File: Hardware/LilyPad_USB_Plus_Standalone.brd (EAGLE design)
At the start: 50.7 x 50.7 mm, 114 parts, among them J1 SEWTAP_LONG-2SIDE, J10 SEWTAP_LONG-2SIDE, J11 SEWTAP_LONG-2SIDE, J12 SEWTAP_LONG-2SIDE, J13 SEWTAP_LONG-2SIDE, J14 SEWTAP_LONG-2SIDE, J15 AMP FCI 10103594-0001LF, J2 SEWTAP_LONG-2SIDE, J3 SEWTAP_LONG-2SIDE, J4 SEWTAP_LONG-2SIDE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

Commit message: Cleaned up some things
Ready for proto review
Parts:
- removed U$51, U$52, U$55, U$56, U$57, U$58, U$59, U$60, U$61, U$62, U$63, U$64, U$65, U$66, U$67: (no value), newLilypadParts:ROUTE_TICKS
- moved LOGO1 6.94 mm to (31.5, 11.4)
- moved LOGO6 6.35 mm to (24.9, 19.3)
- moved C3 1.27 mm to (35.0, 38.8)
- moved C5 1.27 mm to (24.6, 34.8)
- moved C6 1.27 mm to (40.8, 28.7)
- moved J12 1.27 mm to (46.3, 32.2)
- moved J14 1.27 mm to (34.3, 45.5)
- moved J9 1.27 mm to (38.3, 7.60)
- moved JP3 1.27 mm to (41.4, 34.5)
- moved S1 1.27 mm to (37.7, 20.3)
- moved TP7 1.27 mm to (36.2, 14.5)
- moved U$10 1.27 mm to (46.3, 32.2)
- moved U$11 1.27 mm to (46.3, 32.2)
- moved U$24 1.27 mm to (38.3, 7.60)
- moved U$25 1.27 mm to (38.3, 7.60)
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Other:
- board text added: "Inches"
- board text added: "Plated holes: 0.11"
- board text added: "Unplated holes: 0.013"
- board text added: "v01"
- board text removed: "v10"

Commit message: Small changes after Review
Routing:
- net GND: track 38.1 -> 42.7 mm, vias 21 -> 22
- net D3: track 41.7 -> 44.8 mm, vias 2 -> 3
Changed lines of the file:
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@@
 <layer number="47" name="Measures" color="7" fill="1" visible="no" active="yes"/>
 <layer number="48" name="Document" color="7" fill="1" visible="no" active="no"/>
-<layer number="49" name="Reference" color="13" fill="1" visible="no" active="yes"/>
+<layer number="49" name="Reference" color="13" fill="1" visible="yes" active="yes"/>
 <layer number="50" name="dxf" color="7" fill="1" visible="no" active="no"/>
 <layer number="52" name="bDocu" color="7" fill="1" visible="no" active="no"/>
@@
 <wire x1="29.501134375" y1="33.006678125" x2="29.4878125" y2="33.02" width="0.2032" layer="1"/>
 <contactref element="TP5" pad="P$1"/>
+<via x="0.762" y="22.606" extent="1-16" drill="0.3302"/>
+<wire x1="3.550275" y1="23.104434375" x2="1.965328125" y2="23.104434375" width="0.254" layer="16"/>
+<wire x1="0.762" y1="22.606" x2="3.051840625" y2="22.606" width="0.254" layer="16"/>
+<wire x1="3.051840625" y1="22.606" x2="3.550275" y2="23.104434375" width="0.254" layer="16"/>
 </signal>
 <signal name="N$3">
@@
 <wire x1="27.559" y1="39.9415" x2="29.130625" y2="41.513125" width="0.2032" layer="16"/>
 <wire x1="31.958865625" y1="37.6265" x2="31.958865625" y2="38.308865625" width="0.2032" layer="1"/>
+<via x="1.905" y="33.274" extent="1-16" drill="0.3302"/>
+<wire x1="4.496146875" y1="32.2007125" x2="4.50655" y2="32.190309375" width="0.254" layer="16"/>
+<wire x1="1.905" y1="33.274" x2="3.422859375" y2="33.274" width="0.254" layer="16"/>
+<wire x1="3.422859375" y1="33.274" x2="4.50655" y2="32.190309375" width="0.254" layer="16"/>
 </signal>
 <signal name="D9">

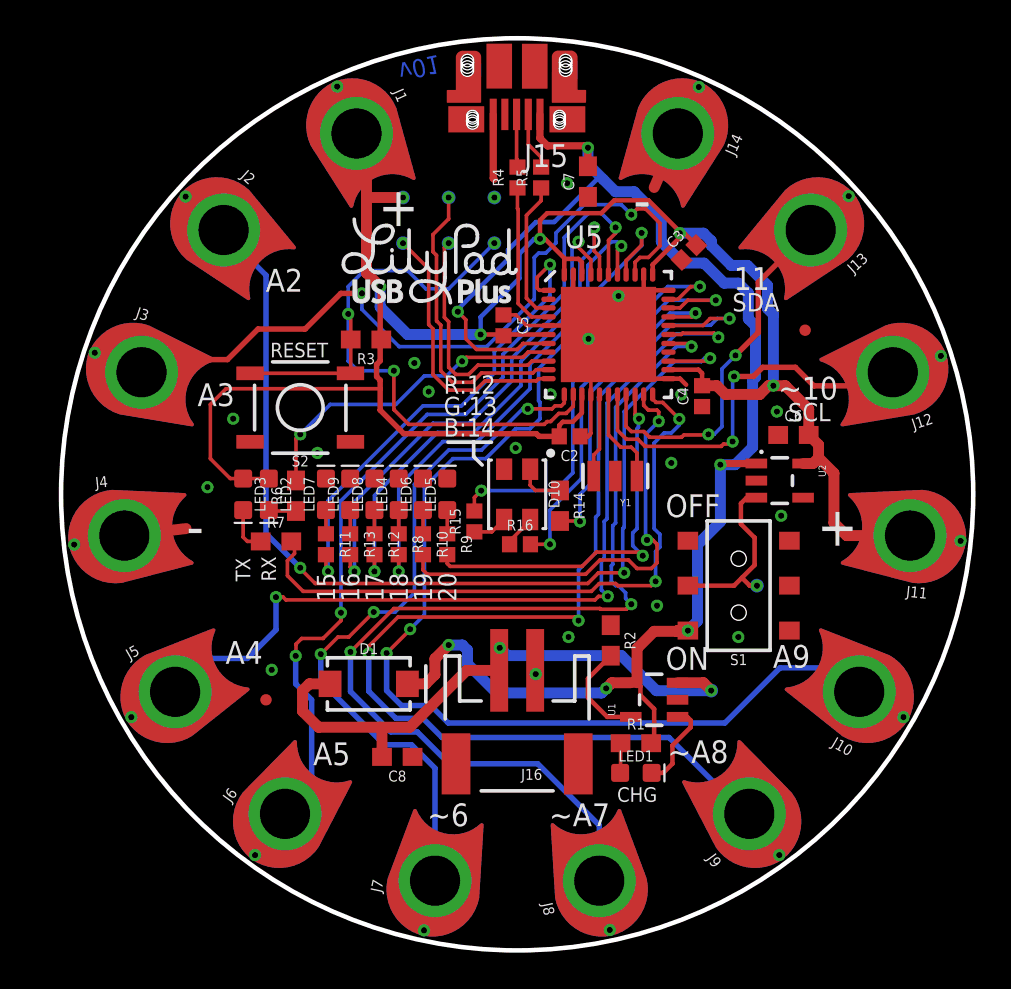
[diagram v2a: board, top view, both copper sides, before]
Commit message: Issues found from my double check
Fiducials on underside placed, Sparkfun name on board changed to flame according to Lilypad design rules.
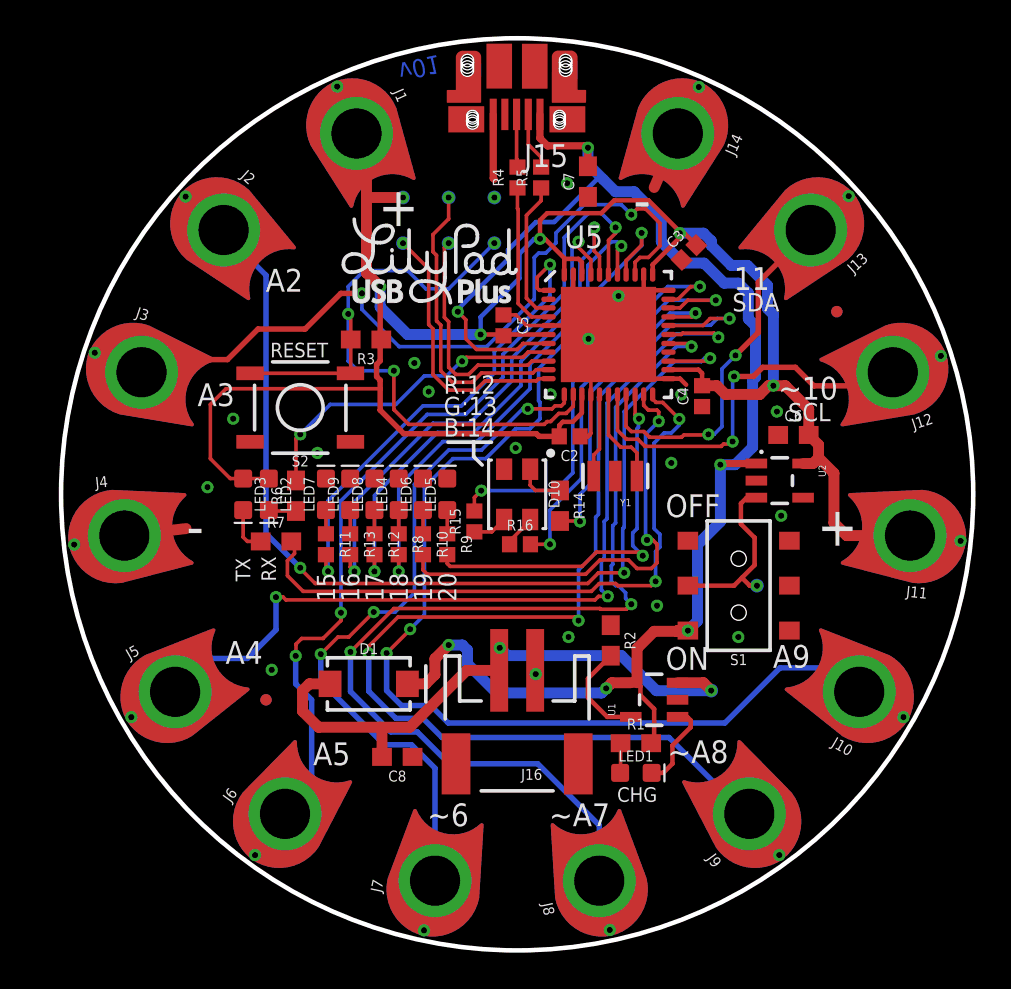
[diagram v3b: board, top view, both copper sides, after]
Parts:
- added JP1, JP4: FIDUCIALUFIDUCIAL, SparkFun:MICRO-FIDUCIAL
- LOGO1: value SFE_LOGO_NAME_FLAME.1_INCH -> SFE_LOGO_FLAME.2_INCH; device SparkFun-Aesthetics:SFE_LOGO_NAME_FLAME_.1 -> SparkFun-Aesthetics:SFE_LOGO_FLAME_.2
- moved LOGO6 12.3 mm to (25.5, 31.6)
- moved LOGO1 9.02 mm to (26.7, 19.1)
- moved JP3 2.04 mm to (43.2, 35.6)
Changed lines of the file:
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@@
 <dimension x1="50.79999375" y1="25.4" x2="0.00000625" y2="25.4" x3="25.4" y3="60.96" textsize="1.778" textratio="15" layer="47" unit="inch"/>
 <text x="29.845" y="61.722" size="1.778" layer="47" font="vector" ratio="15">Inches</text>
-<text x="5.08" y="-14.76375" size="1.778" layer="51" font="vector" align="top-left">LilyPad concept and shapes by:  L. Buechley and N. Seidle</text>
+<text x="-5.08" y="-14.76375" size="1.778" layer="52" font="vector" rot="MR0" align="top-left">LilyPad concept and shapes by:  L. Buechley and N. Seidle</text>
+<text x="-5.08" y="-30.48" size="1.778" layer="52" rot="MR0" align="top-left">PCB thickness: 31 mil / 0.8mm </text>
+<text x="-5.08" y="-34.29" size="1.778" layer="52" rot="MR0" align="top-left">Solder mask color: Purple (Lilypad)</text>
+<text x="-5.08" y="-38.1" size="1.778" layer="52" rot="MR0" align="top-left">Finishing: Lead-free HASL</text>
+<text x="-5.08" y="-41.91" size="1.778" layer="52" rot="MR0" align="top-left">Unplated holes:
+0.013
+</text>
+<text x="-31.75" y="-41.91" size="1.778" layer="52" rot="MR0" align="top-left">Plated holes:
+0.11
+</text>
+<text x="-52.07" y="-11.43" size="1.778" layer="52" font="vector" rot="MR0">Marshall Taylor</text>
+<text x="-32.131" y="-13.97" size="1.778" layer="52" font="vector" rot="MR0">Revised by: Elias Santistevan</text>
+<text x="3.81" y="-14.76375" size="1.778" layer="51" font="vector" align="top-left">LilyPad concept and shapes by:  L. Buechley and N. Seidle</text>
+<text x="50.8" y="-11.43" size="1.778" layer="51" font="vector">Marshall Taylor</text>
+<text x="32.131" y="-13.97" size="1.778" layer="51" font="vector">Revised by: Elias Santistevan</text>
 <text x="5.08" y="-30.48" size="1.778" layer="51" align="top-left">PCB thickness: 31 mil / 0.8mm </text>
 <text x="5.08" y="-34.29" size="1.778" layer="51" align="top-left">Solder mask color: Purple (Lilypad)</text>
@@
 0.11
 </text>
-<text x="52.07" y="-11.43" size="1.778" layer="51" font="vector">Marshall Taylor</text>
-<text x="32.131" y="-13.97" size="1.778" layer="51" font="vector">Revised by: Elias Santistevan</text>
 </plain>
 <attributes>
@@
 </element>
 <element name="JP2" library="SparkFun" package="MICRO-FIDUCIAL" value="FIDUCIALUFIDUCIAL" x="11.430003125" y="13.970003125"/>
-<element name="JP3" library="SparkFun" package="MICRO-FIDUCIAL" value="FIDUCIALUFIDUCIAL" x="41.417871875" y="34.528121875"/>
+<element name="JP3" library="SparkFun" package="MICRO-FIDUCIAL" value="FIDUCIALUFIDUCIAL" x="43.18063125" y="35.5619"/>
 <element name="D1" library="SparkFun-DiscreteSemi" package="SMA-DIODE" value="3A/40V/500mV" x="17.145003125" y="14.859">
 <attribute name="PROD_ID" value="DIO-09886" x="17.145003125" y="14.859" size="1.778" layer="27" display="off"/>
@@
 <element name="U$44" library="SparkFun-Aesthetics" package="ORDERING_INSTRUCTIONS" value="SPECIAL_INSTRUCTIONS-ORDERING" x="3.81" y="-19.05"/>
 <element name="U$1" library="newLilypadParts" package="LILYPAD-WEARABLES_LOGO-LILYPAD" value="LILYLOGO_SHORT" x="25.4" y="27.5828125" rot="MR0"/>
-<element name="LOGO6" library="SparkFun-Aesthetics" package="OSHW-LOGO-S" value="OSHW-LOGOS" x="24.892" y="19.304" rot="MR0"/>
+<element name="LOGO6" library="SparkFun-Aesthetics" package="OSHW-LOGO-S" value="OSHW-LOGOS" x="25.527" y="31.623" rot="MR0"/>
 <element name="D10" library="SparkFun-LED" package="PLCC4SMDLED" value="XZM2CRKM2DGFBB45SCCB" x="25.4" y="25.4" rot="R270">
 <attribute name="PROD_ID" value="DIO-13722" x="25.4" y="25.4" size="1.778" layer="27" rot="R270" display="off"/>
@@
 <element name="TP7" library="SparkFun-Connectors" package="PAD.03X.03" value="TEST-POINT3" x="36.195" y="14.4859375" rot="MR0"/>
 <element name="TP8" library="SparkFun-Connectors" package="PAD.03X.03" value="TEST-POINT3" x="38.735" y="20.32" rot="MR0"/>
-<element name="LOGO1" library="SparkFun-Aesthetics" package="SFE_LOGO_NAME_FLAME_.1" value="SFE_LOGO_NAME_FLAME.1_INCH" x="31.496" y="11.43" rot="MR0"/>
+<element name="JP1" library="SparkFun" package="MICRO-FIDUCIAL" value="FIDUCIALUFIDUCIAL" x="11.43" y="13.97" rot="MR0"/>
+<element name="JP4" library="SparkFun" package="MICRO-FIDUCIAL" value="FIDUCIALUFIDUCIAL" x="43.18" y="35.56" rot="MR0"/>
+<element name="LOGO1" library="SparkFun-Aesthetics" package="SFE_LOGO_FLAME_.2" value="SFE_LOGO_FLAME.2_INCH" x="26.67" y="19.05" rot="MR0"/>
 </elements>
 <signals>

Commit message: Post designe review changes
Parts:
- moved LOGO1 5.16 mm to (27.6, 14.0)
- moved LOGO6 5.08 mm to (25.5, 36.7)
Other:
- board text added: "v10"
- board text removed: "v01"
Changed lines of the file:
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@@
 <layer number="47" name="Measures" color="7" fill="1" visible="no" active="yes"/>
 <layer number="48" name="Document" color="7" fill="1" visible="no" active="no"/>
-<layer number="49" name="Reference" color="13" fill="1" visible="no" active="yes"/>
+<layer number="49" name="Reference" color="13" fill="1" visible="yes" active="yes"/>
 <layer number="50" name="dxf" color="7" fill="1" visible="no" active="no"/>
 <layer number="52" name="bDocu" color="7" fill="1" visible="no" active="no"/>
@@
 <text x="27.178003125" y="6.937378125" size="1.27" layer="21" font="vector" ratio="15">~A7</text>
 <text x="20.399378125" y="6.937378125" size="1.27" layer="21" font="vector" ratio="15">~6</text>
-<text x="18.716628125" y="49.355371875" size="1.016" layer="16" font="vector" ratio="15" rot="SMR167.6">v01</text>
+<text x="26.622371875" y="7.413628125" size="1.016" layer="16" font="vector" ratio="15" rot="SMR0">v10</text>
 <text x="42.084628125" y="22.54249375" size="2.1844" layer="21" font="vector" ratio="15">+</text>
 <text x="37.449121875" y="36.76649375" size="1.27" layer="21" font="vector" ratio="15">11</text>
@@
 <text x="-52.07" y="-11.43" size="1.778" layer="52" font="vector" rot="MR0">Marshall Taylor</text>
 <text x="-32.131" y="-13.97" size="1.778" layer="52" font="vector" rot="MR0">Revised by: Elias Santistevan</text>
-<text x="3.81" y="-14.76375" size="1.778" layer="51" font="vector" align="top-left">LilyPad concept and shapes by:  L. Buechley and N. Seidle</text>
+<text x="-3.81" y="-14.76375" size="1.778" layer="52" font="vector" rot="MR0" align="top-left">LilyPad concept and shapes by:  L. Buechley and N. Seidle</text>
+<text x="-50.8" y="-11.43" size="1.778" layer="52" font="vector" rot="MR0">Marshall Taylor</text>
+<text x="-32.131" y="-13.97" size="1.778" layer="52" font="vector" rot="MR0">Revised by: Elias Santistevan</text>
+<text x="-5.08" y="-30.48" size="1.778" layer="52" rot="MR0" align="top-left">PCB thickness: 31 mil / 0.8mm </text>
+<text x="-5.08" y="-34.29" size="1.778" layer="52" rot="MR0" align="top-left">Solder mask color: Purple (Lilypad)</text>
+<text x="-5.08" y="-38.1" size="1.778" layer="52" rot="MR0" align="top-left">Finishing: Lead-free HASL</text>
+<text x="-5.08" y="-41.91" size="1.778" layer="52" rot="MR0" align="top-left">Unplated holes:
+0.013
+</text>
+<text x="-31.75" y="-41.91" size="1.778" layer="52" rot="MR0" align="top-left">Plated holes:
+0.11
+</text>
+<text x="-151.13" y="-29.21" size="1.778" layer="52" rot="MR0" align="top-left">PCB thickness: 31 mil / 0.8mm </text>
+<text x="-151.13" y="-33.02" size="1.778" layer="52" rot="MR0" align="top-left">Solder mask color: Purple (Lilypad)</text>
+<text x="-151.13" y="-36.83" size="1.778" layer="52" rot="MR0" align="top-left">Finishing: Lead-free HASL</text>
+<text x="-151.13" y="-40.64" size="1.778" layer="52" rot="MR0" align="top-left">Unplated holes:
+0.013
+</text>
+<text x="-177.8" y="-40.64" size="1.778" layer="52" rot="MR0" align="top-left">Plated holes:
+0.11
+</text>
+<text x="-154.94" y="-20.32" size="1.778" layer="52" font="vector" rot="MR0">Marshall Taylor</text>
+<text x="-141.351" y="-24.13" size="1.778" layer="52" font="vector" rot="MR0">Revised by: Elias Santistevan</text>
+<text x="-142.24" y="-26.19375" size="1.778" layer="52" font="vector" rot="MR0" align="top-left">LilyPad concept and shapes by:  L. Buechley and N. Seidle</text>
+<text x="5.08" y="-29.21" size="1.778" layer="51" align="top-left">PCB thickness: 31 mil / 0.8mm </text>
+<text x="5.08" y="-33.02" size="1.778" layer="51" align="top-left">Solder mask color: Purple (Lilypad)</text>
+<text x="5.08" y="-36.83" size="1.778" layer="51" align="top-left">Finishing: Lead-free HASL</text>
+<text x="5.08" y="-40.64" size="1.778" layer="51" align="top-left">Unplated holes:
+0.013
+</text>
+<text x="31.75" y="-40.64" size="1.778" layer="51" align="top-left">Plated holes:
+0.11
+</text>
 <text x="50.8" y="-11.43" size="1.778" layer="51" font="vector">Marshall Taylor</text>
 <text x="32.131" y="-13.97" size="1.778" layer="51" font="vector">Revised by: Elias Santistevan</text>
-<text x="5.08" y="-30.48" size="1.778" layer="51" align="top-left">PCB thickness: 31 mil / 0.8mm </text>
-<text x="5.08" y="-34.29" size="1.778" layer="51" align="top-left">Solder mask color: Purple (Lilypad)</text>
-<text x="5.08" y="-38.1" size="1.778" layer="51" align="top-left">Finishing: Lead-free HASL</text>
-<text x="5.08" y="-41.91" size="1.778" layer="51" align="top-left">Unplated holes:
-0.013
-</text>
-<text x="31.75" y="-41.91" size="1.778" layer="51" align="top-left">Plated holes:
-0.11
-</text>
+<text x="3.81" y="-16.03375" size="1.778" layer="51" font="vector" align="top-left">LilyPad concept and shapes by:  L. Buechley and N. Seidle</text>
 </plain>
 <attributes>
@@
 <element name="U$44" library="SparkFun-Aesthetics" package="ORDERING_INSTRUCTIONS" value="SPECIAL_INSTRUCTIONS-ORDERING" x="3.81" y="-19.05"/>
 <element name="U$1" library="newLilypadParts" package="LILYPAD-WEARABLES_LOGO-LILYPAD" value="LILYLOGO_SHORT" x="25.4" y="27.5828125" rot="MR0"/>
-<element name="LOGO6" library="SparkFun-Aesthetics" package="OSHW-LOGO-S" value="OSHW-LOGOS" x="25.527" y="31.623" rot="MR0"/>
+<element name="LOGO6" library="SparkFun-Aesthetics" package="OSHW-LOGO-S" value="OSHW-LOGOS" x="25.527" y="36.703" rot="MR0"/>
 <element name="D10" library="SparkFun-LED" package="PLCC4SMDLED" value="XZM2CRKM2DGFBB45SCCB" x="25.4" y="25.4" rot="R270">
 <attribute name="PROD_ID" value="DIO-13722" x="25.4" y="25.4" size="1.778" layer="27" rot="R270" display="off"/>
@@
 <element name="JP1" library="SparkFun" package="MICRO-FIDUCIAL" value="FIDUCIALUFIDUCIAL" x="11.43" y="13.97" rot="MR0"/>
 <element name="JP4" library="SparkFun" package="MICRO-FIDUCIAL" value="FIDUCIALUFIDUCIAL" x="43.18" y="35.56" rot="MR0"/>
-<element name="LOGO1" library="SparkFun-Aesthetics" package="SFE_LOGO_FLAME_.2" value="SFE_LOGO_FLAME.2_INCH" x="26.67" y="19.05" rot="MR0"/>
+<element name="LOGO1" library="SparkFun-Aesthetics" package="SFE_LOGO_FLAME_.2" value="SFE_LOGO_FLAME.2_INCH" x="27.559" y="13.97" rot="MR0"/>
 </elements>
 <signals>

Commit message: Changes after double check
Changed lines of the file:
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@@
 <layer number="47" name="Measures" color="7" fill="1" visible="no" active="yes"/>
 <layer number="48" name="Document" color="7" fill="1" visible="no" active="no"/>
-<layer number="49" name="Reference" color="13" fill="1" visible="yes" active="yes"/>
+<layer number="49" name="Reference" color="13" fill="1" visible="no" active="yes"/>
 <layer number="50" name="dxf" color="7" fill="1" visible="no" active="no"/>
 <layer number="52" name="bDocu" color="7" fill="1" visible="no" active="no"/>
@@
 </polygon>
 <text x="-31.75" y="-13.97" size="1.778" layer="52" font="vector" rot="MR0">Revised by: Elias Santistevan</text>
-<circle x="25.4" y="25.4" radius="25.368509375" width="0.254" layer="20"/>
+<circle x="25.4" y="25.4" radius="25.368509375" width="0.2032" layer="20"/>
 <dimension x1="50.79999375" y1="25.4" x2="0.00000625" y2="25.4" x3="25.4" y3="60.96" textsize="1.778" textratio="15" layer="47" unit="inch"/>
 <text x="29.845" y="61.722" size="1.778" layer="47" font="vector" ratio="15">Inches</text>
